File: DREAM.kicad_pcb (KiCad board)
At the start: 2 copper layers, 100 x 60 mm, 134 parts, among them J401 KLDX-0202-B, J402 EBWA-02-B, J501 USB4105-GF-A, J502 TC2030-CTX, J601 1-1337535-0, J602 1-1337535-0, J603 1-1337535-0, J701 PH1-02-UA, Q401 MCU18P10Y-TP, SW501 PTS526SK15SMTR2 LFS, U401 TPS7A2030PDBVR, U501 USBLC6-2SC6, U502 STM32G441KBT6, U601 TSV912AIDR, U602 TSV912AIDR, U603 LM358LVIDR, U604 TSV912AIDR, U605 TSV912AIDR, U701 LM358LVIDR, U702 LM358LVIDR, Y501 ATS08A-E

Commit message: feat: checked REV A
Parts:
- removed the J502 at (217.3, 153.2)
- added F501: MF-MSMF030-2, Resistor_SMD:R_1812_4532Metric, F.Cu at (251.4, 142.2)
- added FB501: MH1608-601Y, Inductor_SMD:L_0603_1608Metric, F.Cu at (226.6, 158.1)
- added J501: Conn_ST_STDC14, Connector_PinHeader_1.27mm:PinHeader_2x07_P1.27mm_Vertical_SMD, F.Cu at (215.8, 153.6)
- added R709: 100, Resistor_SMD:R_0603_1608Metric, F.Cu at (222.1, 107.9)
- moved R504 10.5 mm to (223.6, 151.6), turned to -45 degrees
- moved R506 9.02 mm to (223.9, 154.6), turned to -45 degrees
- moved C505 7.68 mm to (248.9, 135.2)
- moved R503 7.55 mm to (221.7, 152.4), turned to -45 degrees
- moved C508 7.51 mm to (248.9, 138.4)
- moved TP404 7.18 mm to (243.8, 143.4)
- moved R505 6.16 mm to (225.9, 153.8)
- moved R615 4.38 mm to (219.8, 145.9)
- moved R619 4.38 mm to (221.5, 144.2)
- moved D501 4.01 mm to (201.7, 159.3)
- moved D502 4.01 mm to (201.7, 155.5)
- moved R501 4.01 mm to (205.5, 159.3)
- moved R502 4.01 mm to (205.5, 155.5)
- moved D503 3.00 mm to (258.0, 139.6)
- moved SW501 2.54 mm to (191.1, 158.1)
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- renumbered C506 to C504, C504 to C505, C507 to C506, C508 to C507, C505 to C508, C515 to C510, C516 to C511, C510 to C512, C708 to C707, J501 to J502, R510 to R503, R509 to R504, R507 to R505, R508 to R506, R503 to R507, R505 to R508, R504 to R509, R506 to R510, U502 to U501, U501 to U502
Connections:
- net /PROJECT ARCHITECTURE/ANALOGUE INPUTS/ADC_CE renamed /ARCHITECTURE/ANALOGUE INPUTS/ADC_CE
- net /PROJECT ARCHITECTURE/ANALOGUE INPUTS/ADC_CO2 renamed /ARCHITECTURE/ANALOGUE INPUTS/ADC_CO2
- net /PROJECT ARCHITECTURE/ANALOGUE INPUTS/ADC_ECG renamed /ARCHITECTURE/ANALOGUE INPUTS/ADC_ECG
- net /PROJECT ARCHITECTURE/ANALOGUE INPUTS/CE_BUFF renamed /ARCHITECTURE/ANALOGUE INPUTS/CE_BUFF
- net /PROJECT ARCHITECTURE/ANALOGUE INPUTS/CE_BUFF_IN renamed /ARCHITECTURE/ANALOGUE INPUTS/CE_BUFF_IN
- net /PROJECT ARCHITECTURE/ANALOGUE INPUTS/CE_FILT renamed /ARCHITECTURE/ANALOGUE INPUTS/CE_FILT
- net /PROJECT ARCHITECTURE/ANALOGUE INPUTS/CE_IN renamed /ARCHITECTURE/ANALOGUE INPUTS/CE_IN
- net /PROJECT ARCHITECTURE/ANALOGUE INPUTS/CE_SK_MID renamed /ARCHITECTURE/ANALOGUE INPUTS/CE_SK_MID
- net /PROJECT ARCHITECTURE/ANALOGUE INPUTS/CE_SK_N renamed /ARCHITECTURE/ANALOGUE INPUTS/CE_SK_N
- net /PROJECT ARCHITECTURE/ANALOGUE INPUTS/CE_SK_RC renamed /ARCHITECTURE/ANALOGUE INPUTS/CE_SK_RC
- net /PROJECT ARCHITECTURE/ANALOGUE INPUTS/CO2_BUFF renamed /ARCHITECTURE/ANALOGUE INPUTS/CO2_BUFF
- net /PROJECT ARCHITECTURE/ANALOGUE INPUTS/CO2_BUFF_IN renamed /ARCHITECTURE/ANALOGUE INPUTS/CO2_BUFF_IN
- net /PROJECT ARCHITECTURE/ANALOGUE INPUTS/CO2_FILT renamed /ARCHITECTURE/ANALOGUE INPUTS/CO2_FILT
- net /PROJECT ARCHITECTURE/ANALOGUE INPUTS/CO2_GAIN_N renamed /ARCHITECTURE/ANALOGUE INPUTS/CO2_GAIN_N
- net /PROJECT ARCHITECTURE/ANALOGUE INPUTS/CO2_IN renamed /ARCHITECTURE/ANALOGUE INPUTS/CO2_IN
- net /PROJECT ARCHITECTURE/ANALOGUE INPUTS/CO2_OUT renamed /ARCHITECTURE/ANALOGUE INPUTS/CO2_OUT
- net /PROJECT ARCHITECTURE/ANALOGUE INPUTS/CO2_SK_MID renamed /ARCHITECTURE/ANALOGUE INPUTS/CO2_SK_MID
- net /PROJECT ARCHITECTURE/ANALOGUE INPUTS/CO2_SK_RC renamed /ARCHITECTURE/ANALOGUE INPUTS/CO2_SK_RC
- net /PROJECT ARCHITECTURE/ANALOGUE INPUTS/ECG_FILT renamed /ARCHITECTURE/ANALOGUE INPUTS/ECG_FILT
- net /PROJECT ARCHITECTURE/ANALOGUE INPUTS/ECG_GAIN_N renamed /ARCHITECTURE/ANALOGUE INPUTS/ECG_GAIN_N
- net /PROJECT ARCHITECTURE/ANALOGUE INPUTS/ECG_IN renamed /ARCHITECTURE/ANALOGUE INPUTS/ECG_IN
- net /PROJECT ARCHITECTURE/ANALOGUE INPUTS/ECG_LPF1 renamed /ARCHITECTURE/ANALOGUE INPUTS/ECG_LPF1
- net /PROJECT ARCHITECTURE/ANALOGUE INPUTS/ECG_LPF1_N renamed /ARCHITECTURE/ANALOGUE INPUTS/ECG_LPF1_N
- net /PROJECT ARCHITECTURE/ANALOGUE INPUTS/ECG_OUT renamed /ARCHITECTURE/ANALOGUE INPUTS/ECG_OUT
- net /PROJECT ARCHITECTURE/ANALOGUE INPUTS/ECG_SK_MID renamed /ARCHITECTURE/ANALOGUE INPUTS/ECG_SK_MID
- net /PROJECT ARCHITECTURE/ANALOGUE INPUTS/ECG_SK_RC renamed /ARCHITECTURE/ANALOGUE INPUTS/ECG_SK_RC
- net /PROJECT ARCHITECTURE/ANALOGUE INPUTS/SERVO_N renamed /ARCHITECTURE/ANALOGUE INPUTS/SERVO_N
- net /PROJECT ARCHITECTURE/ANALOGUE INPUTS/SERVO_OUT renamed /ARCHITECTURE/ANALOGUE INPUTS/SERVO_OUT
- net /PROJECT ARCHITECTURE/ANALOGUE INPUTS/SERVO_P renamed /ARCHITECTURE/ANALOGUE INPUTS/SERVO_P
- net /PROJECT ARCHITECTURE/ANALOGUE OUTPUTS/DAC_SHAKER renamed /ARCHITECTURE/ANALOGUE OUTPUTS/DAC_SHAKER
- net /PROJECT ARCHITECTURE/ANALOGUE OUTPUTS/SHAKER_N renamed /ARCHITECTURE/ANALOGUE OUTPUTS/SHAKER_N
- net /PROJECT ARCHITECTURE/ANALOGUE OUTPUTS/SHAKER_P renamed /ARCHITECTURE/ANALOGUE OUTPUTS/SHAKER_P
- net /PROJECT ARCHITECTURE/ANALOGUE OUTPUTS/SHK_FILT1 renamed /ARCHITECTURE/ANALOGUE OUTPUTS/SHK_FILT1
- net /PROJECT ARCHITECTURE/ANALOGUE OUTPUTS/SHK_FILT2 renamed /ARCHITECTURE/ANALOGUE OUTPUTS/SHK_FILT2
- net /PROJECT ARCHITECTURE/ANALOGUE OUTPUTS/SHK_N renamed /ARCHITECTURE/ANALOGUE OUTPUTS/SHK_N
- net /PROJECT ARCHITECTURE/ANALOGUE OUTPUTS/SHK_SK1_MID renamed /ARCHITECTURE/ANALOGUE OUTPUTS/SHK_SK1_MID
- net /PROJECT ARCHITECTURE/ANALOGUE OUTPUTS/SHK_SK1_RC renamed /ARCHITECTURE/ANALOGUE OUTPUTS/SHK_SK1_RC
- net /PROJECT ARCHITECTURE/ANALOGUE OUTPUTS/SHK_SK2_MID renamed /ARCHITECTURE/ANALOGUE OUTPUTS/SHK_SK2_MID
- net /PROJECT ARCHITECTURE/ANALOGUE OUTPUTS/SHK_SK2_RC renamed /ARCHITECTURE/ANALOGUE OUTPUTS/SHK_SK2_RC
- net /PROJECT ARCHITECTURE/ANALOGUE OUTPUTS/VREF_SHK renamed /ARCHITECTURE/ANALOGUE OUTPUTS/VREF_SHK
- net /PROJECT ARCHITECTURE/DIGITAL AND HMI/A+ renamed /ARCHITECTURE/DIGITAL AND HMI/A+
- net /PROJECT ARCHITECTURE/DIGITAL AND HMI/A- renamed /ARCHITECTURE/DIGITAL AND HMI/A-
- net /PROJECT ARCHITECTURE/DIGITAL AND HMI/BTN renamed /ARCHITECTURE/DIGITAL AND HMI/BTN
- net /PROJECT ARCHITECTURE/DIGITAL AND HMI/CC1 renamed /ARCHITECTURE/DIGITAL AND HMI/CC1
- net /PROJECT ARCHITECTURE/DIGITAL AND HMI/CC2 renamed /ARCHITECTURE/DIGITAL AND HMI/CC2
- net /PROJECT ARCHITECTURE/DIGITAL AND HMI/D+ renamed /ARCHITECTURE/DIGITAL AND HMI/D+
- net /PROJECT ARCHITECTURE/DIGITAL AND HMI/D- renamed /ARCHITECTURE/DIGITAL AND HMI/D-
- net /PROJECT ARCHITECTURE/DIGITAL AND HMI/LED_GRN renamed /ARCHITECTURE/DIGITAL AND HMI/LED_GRN
- net /PROJECT ARCHITECTURE/DIGITAL AND HMI/LED_RED renamed /ARCHITECTURE/DIGITAL AND HMI/LED_RED
- net /PROJECT ARCHITECTURE/DIGITAL AND HMI/OSC_IN renamed /ARCHITECTURE/DIGITAL AND HMI/OSC_IN
- net /PROJECT ARCHITECTURE/DIGITAL AND HMI/OSC_OUT renamed /ARCHITECTURE/DIGITAL AND HMI/OSC_OUT
- net /PROJECT ARCHITECTURE/DIGITAL AND HMI/SWCLK renamed /ARCHITECTURE/DIGITAL AND HMI/SWCLK
- net /PROJECT ARCHITECTURE/DIGITAL AND HMI/SWDIO renamed /ARCHITECTURE/DIGITAL AND HMI/SWDIO
- net /PROJECT ARCHITECTURE/DIGITAL AND HMI/SWO renamed /ARCHITECTURE/DIGITAL AND HMI/SWO
- net /PROJECT ARCHITECTURE/DIGITAL AND HMI/VDDA renamed /ARCHITECTURE/DIGITAL AND HMI/VDDA
- net /PROJECT ARCHITECTURE/DIGITAL AND HMI/XTAL renamed /ARCHITECTURE/DIGITAL AND HMI/XTAL
- net /PROJECT ARCHITECTURE/DIGITAL AND HMI/~{RST} renamed /ARCHITECTURE/DIGITAL AND HMI/~{RST}
- net /PROJECT ARCHITECTURE/POWER/GATE_RPP renamed /ARCHITECTURE/POWER/GATE_RPP
- net /PROJECT ARCHITECTURE/POWER/VBATT_FUSED renamed /ARCHITECTURE/POWER/VBATT_FUSED
- net /PROJECT ARCHITECTURE/POWER/VBATT_RAW renamed /ARCHITECTURE/POWER/VBATT_RAW
- J502 pad A4: VBUS -> /ARCHITECTURE/DIGITAL AND HMI/VBUS_RAW
- J502 pad A9: VBUS -> /ARCHITECTURE/DIGITAL AND HMI/VBUS_RAW
- J502 pad B4: VBUS -> /ARCHITECTURE/DIGITAL AND HMI/VBUS_RAW
- J502 pad B9: VBUS -> /ARCHITECTURE/DIGITAL AND HMI/VBUS_RAW
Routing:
- net /ARCHITECTURE/DIGITAL AND HMI/SWDIO: track 36.3 -> 17.8 mm
- net /ARCHITECTURE/DIGITAL AND HMI/SWCLK: track 29.0 -> 18.1 mm
- net Net-(J501-~{RST}): track 2.49 -> 12.1 mm
- net /ARCHITECTURE/DIGITAL AND HMI/SWO: track 24.4 -> 15.2 mm
- net Net-(J501-JTMS/SWDIO): track 2.78 -> 9.44 mm
- net /ARCHITECTURE/DIGITAL AND HMI/~{RST}: track 27.8 -> 21.1 mm
- net /ARCHITECTURE/DIGITAL AND HMI/OSC_IN: track 3.81 -> 9.25 mm
- net /ARCHITECTURE/DIGITAL AND HMI/LED_RED: track 38.9 -> 44.0 mm
- net Net-(J501-JTDO/SWO): track 2.78 -> 7.84 mm
- net /ARCHITECTURE/ANALOGUE INPUTS/CO2_OUT: track 32.9 -> 28.4 mm
- net /ARCHITECTURE/ANALOGUE INPUTS/ADC_CO2: track 3.25 -> 7.65 mm
- net /ARCHITECTURE/ANALOGUE INPUTS/CE_FILT: track 47.3 -> 43.0 mm
- net /ARCHITECTURE/ANALOGUE INPUTS/ADC_CE: track 6.07 -> 10.4 mm
- net /ARCHITECTURE/DIGITAL AND HMI/BTN: track 54.4 -> 58.4 mm
- net /ARCHITECTURE/DIGITAL AND HMI/LED_GRN: track 38.6 -> 42.6 mm
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- added copper zone on F.Cu, net /ARCHITECTURE/DIGITAL AND HMI/VBUS_RAW
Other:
- board text added: "D503"
- board text added: "SW501"

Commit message: fix: schem and fab document
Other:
- board text removed: "D503"
- board text removed: "SW501"
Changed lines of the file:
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@@
 	)
 	(gr_rect
+		(start 219.2944 103.6228)
+		(end 225.3396 107.128)
+		(stroke
+			(width 0.15)
+			(type solid)
+		)
+		(fill no)
+		(layer "B.SilkS")
+	)
+	(gr_rect
 		(start 254 128.5)
 		(end 261.75 136.5)
@@
 		(layer "Dwgs.User")
 	)
-	(gr_line
-		(start 240.5 105.3)
-		(end 244.5 107.3)
-		(stroke
-			(width 0.15)
-			(type default)
-		)
-		(layer "Eco1.User")
-	)
-	(gr_rect
-		(start 254.245001 137.39)
-		(end 261.745001 141.89)
-		(stroke
-			(width 0.15)
-			(type default)
-		)
-		(fill no)
-		(layer "Eco1.User")
-	)
-	(gr_line
-		(start 223.5616 107.128)
-		(end 220.6152 108.6012)
-		(stroke
-			(width 0.15)
-			(type default)
-		)
-		(layer "Eco1.User")
-	)
-	(gr_rect
-		(start 220.6152 107.128)
-		(end 223.5616 108.6012)
-		(stroke
-			(width 0.15)
-			(type default)
-		)
-		(fill no)
-		(layer "Eco1.User")
-	)
-	(gr_line
-		(start 261.745001 137.39)
-		(end 254.245001 141.89)
-		(stroke
-			(width 0.15)
-			(type default)
-		)
-		(layer "Eco1.User")
-	)
-	(gr_line
-		(start 220.6152 107.128)
-		(end 223.5616 108.6012)
-		(stroke
-			(width 0.15)
-			(type default)
-		)
-		(layer "Eco1.User")
-	)
-	(gr_line
-		(start 254.245001 137.39)
-		(end 261.745001 141.89)
-		(stroke
-			(width 0.15)
-			(type default)
-		)
-		(layer "Eco1.User")
-	)
-	(gr_rect
-		(start 240.5 105.3)
-		(end 244.5 107.3)
-		(stroke
-			(width 0.15)
-			(type default)
-		)
-		(fill no)
-		(layer "Eco1.User")
-	)
-	(gr_line
-		(start 244.5 105.3)
-		(end 240.5 107.3)
-		(stroke
-			(width 0.15)
-			(type default)
-		)
-		(layer "Eco1.User")
-	)
 	(gr_arc
 		(start 167.5 162.5)
@@
 	)
 	(gr_text "V+"
-		(at 219.142 104.715 180)
+		(at 219.2436 104.7404 180)
 		(layer "F.SilkS" knockout)
 		(effects
@@
 	)
 	(gr_text "V-"
-		(at 225.365 104.715 180)
+		(at 225.238 104.7404 180)
 		(layer "F.SilkS" knockout)
 		(effects
@@
 	)
 	(gr_text "V-"
-		(at 253.75 134.56 90)
+		(at 225.238 104.7404 180)
+		(layer "B.SilkS" knockout)
+		(effects
+			(font
+				(size 1 1)
+				(thickness 0.15)
+			)
+			(justify right)
+		)
+	)
+	(gr_text "V+"
+		(at 219.2436 104.7404 180)
+		(layer "B.SilkS" knockout)
+		(effects
+			(font
+				(size 1 1)
+				(thickness 0.15)
+			)
+			(justify left)
+		)
+	)
+	(gr_text "V-"
+		(at 253.8892 134.56 90)
 		(layer "B.SilkS" knockout)
 		(effects
@@
 	)
 	(gr_text "V+"
-		(at 253.75 130.75 90)
+		(at 253.8892 130.75 90)
 		(layer "B.SilkS" knockout)
 		(effects
@@
 		)
 	)
-	(gr_text "D503"
-		(at 261 139.64 90)
-		(layer "F.Fab")
-		(effects
-			(font
-				(size 1 1)
-				(thickness 0.15)
-			)
-		)
-	)
-	(gr_text "SW501"
-		(at 191.075 158.055 0)
-		(layer "F.Fab")
-		(effects
-			(font
-				(size 0.75 0.75)
-				(thickness 0.15)
-			)
-		)
-	)
 	(gr_text ""
 		(at 72.545008 54.5 0)
@@
 		)
 	)
-	(gr_text "X"
-		(at 107.5 120 0)
-		(layer "User.9")
-		(effects
-			(font
-				(face "Arial")
-				(size 1.27 1.27)
-				(thickness 0.15)
-			)
-		)
-		(render_cache "X" 0
-			(polygon
-				(pts
-					(xy 106.915373 120.52705) (xy 107.407254 119.862316) (xy 106.973456 119.251555) (xy 107.173915 119.251555)
-					(xy 107.404617 119.577795) (xy 107.507057 119.733898) (xy 107.552406 119.664486) (xy 107.607636 119.58904)
-					(xy 107.863619 119.251555) (xy 108.04663 119.251555) (xy 107.599881 119.852777) (xy 108.081371 120.52705)
-					(xy 107.873157 120.52705) (xy 107.553043 120.073321) (xy 107.497519 119.98833) (xy 107.436722 120.083713)
-					(xy 107.117461 120.52705)
-				)
-			)
-		)
-	)
 	(gr_text_box ""
 		(start 23 47)
@@
 	)
 	(group ""
-		(members "d3af8614-f4f5-4154-b789-7cd4c2ee044d")
+		(members "4f4c9daa-413b-49a2-a321-7b0aa535b770" "b65ea624-1492-4667-a13f-5e9fdedb6462")
 	)
 	(group ""
-		(members "4f4c9daa-413b-49a2-a321-7b0aa535b770" "79cc9333-ba3a-4e04-aa78-63a6865dc3a4"
-			"b65ea624-1492-4667-a13f-5e9fdedb6462"
-		)
+		(members "d3af8614-f4f5-4154-b789-7cd4c2ee044d")
 	)
 	(group ""
-		(members "5fa22c35-bc3b-4d84-aaed-ac3a88b89709" "c415e99b-7d1f-44ca-ab10-cfca4af8873b")
+		(members "5fa22c35-bc3b-4d84-aaed-ac3a88b89709" "a7b35efb-2ab1-412b-870c-4cd501f92443")
 	)
 	(group ""
@@
 		(members "30ea6013-eb0f-48ca-a65b-bacfb90e1e0d")
 	)
-	(group ""
-		(members "1e2d455f-f3b1-4c6f-8d60-631d601c44bf" "2c762f2e-1b91-429c-8e6c-24e3a70519bf"
-			"9ad60182-c314-43ef-ba6c-4dbbe5a31389"
-		)
-	)
-	(group ""
-		(members "3fcccba2-a9f8-4d8b-a6a9-da722d1a9218")
-	)
-	(group ""
-		(members "172dfff8-4cf1-4bab-b9a0-c8a083434e90" "f0d9e6bb-a84b-499b-bf6c-1aa18b742c50"
-			"fca67cb9-d931-4ff2-84a9-bf7dcd183cbc"
-		)
-	)
-	(group ""
-		(members "17869f7c-2dd8-4eaf-9f93-e94e5fe2060a" "3c90bb06-ad6b-4678-87d2-fad2acfbdfbd"
-			"bb342e1c-f4a8-4e7b-8866-37dc66ef2c1d"
-		)
-	)
 	(group "kibot_table_csv_drill_table"

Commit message: Update Outputs (release)
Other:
- board text added: "0.02mm"
- board text added: "0.035mm (1.00oz)"
- board text added: "1.49mm"
- board text added: "B.Mask"
- board text added: "B.Paste"
- board text added: "B.Silkscreen"
- board text added: "Copper"
- board text added: "Core"
- board text added: "Dielectric"
- board text added: "Direct Printing"
- board text added: "F.Mask"
- board text added: "F.Paste"
- board text added: "F.Silkscreen"
- board text added: "FR4_7628"
- board text added: "GBR"
- board text added: "Gerber"
- board text added: "L1 (Sig, PWR)"
- board text added: "L2 (Sig, GND)"
- board text added: "Layer"
- board text added: "Legend"
- board text added: "Material"
- board text added: "Note: external layer thicknesses are specified after plating"
- board text added: "Paste Mask"
- board text added: "Plane"
- board text added: "Signal"
- board text added: "Solder Mask"
- board text added: "Solder Resist"
- board text added: "Thickness"
- board text added: "Total thickness: 1.6mm"
- board text added: "Type"

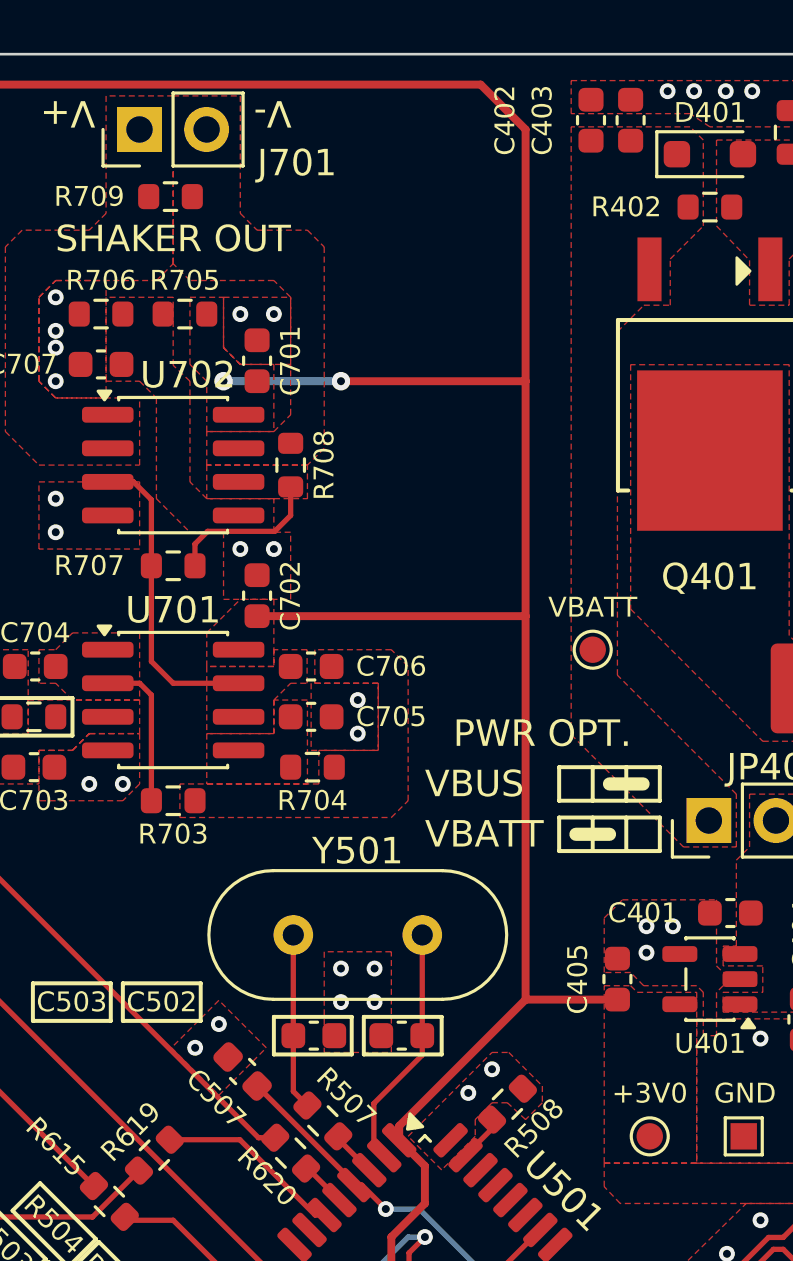
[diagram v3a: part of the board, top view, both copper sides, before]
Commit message: fix: ground under XTAL, untent vias, production files
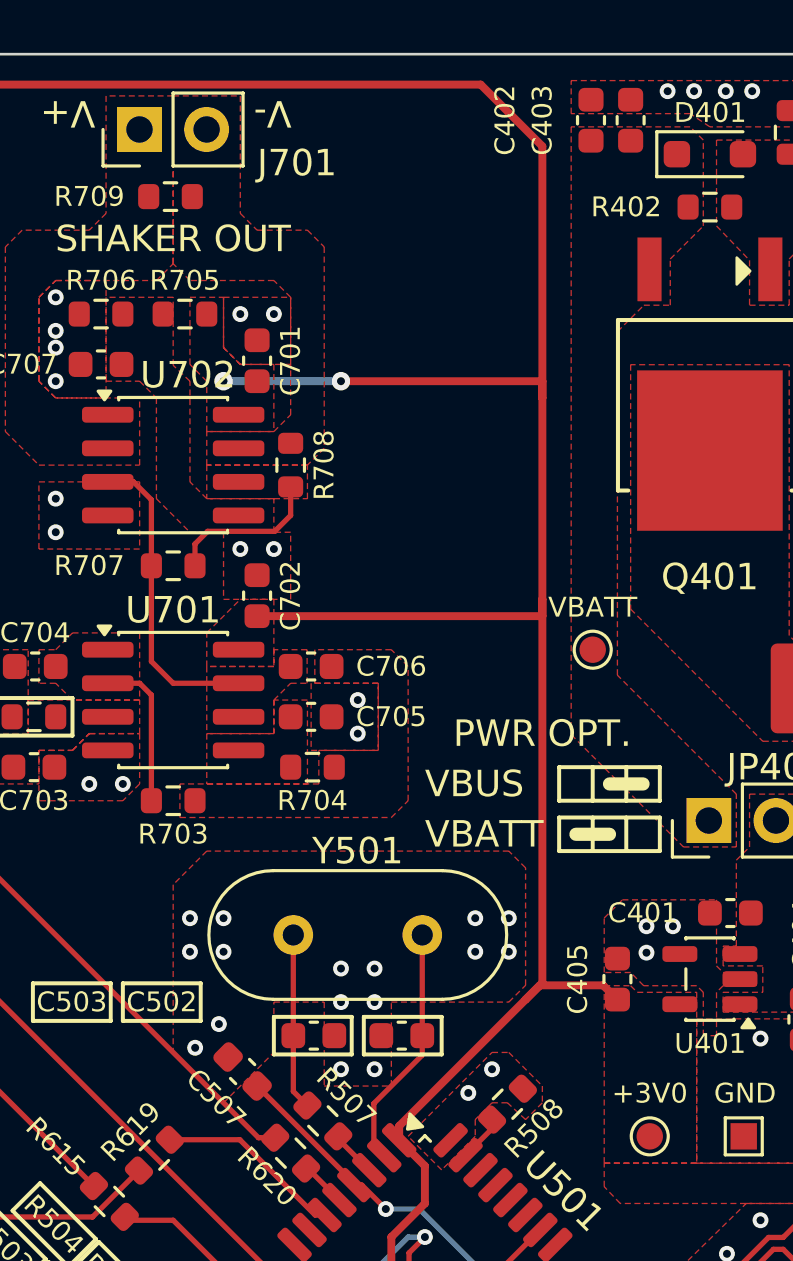
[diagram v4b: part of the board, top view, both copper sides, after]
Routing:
- net +3V0: track 261.1 -> 264.6 mm
- net GND: vias 116 -> 126
